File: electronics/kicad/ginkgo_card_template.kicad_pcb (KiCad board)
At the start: 4 copper layers, 100 x 100 mm, 6 parts, among them J1 GK-P, J2 GK-D

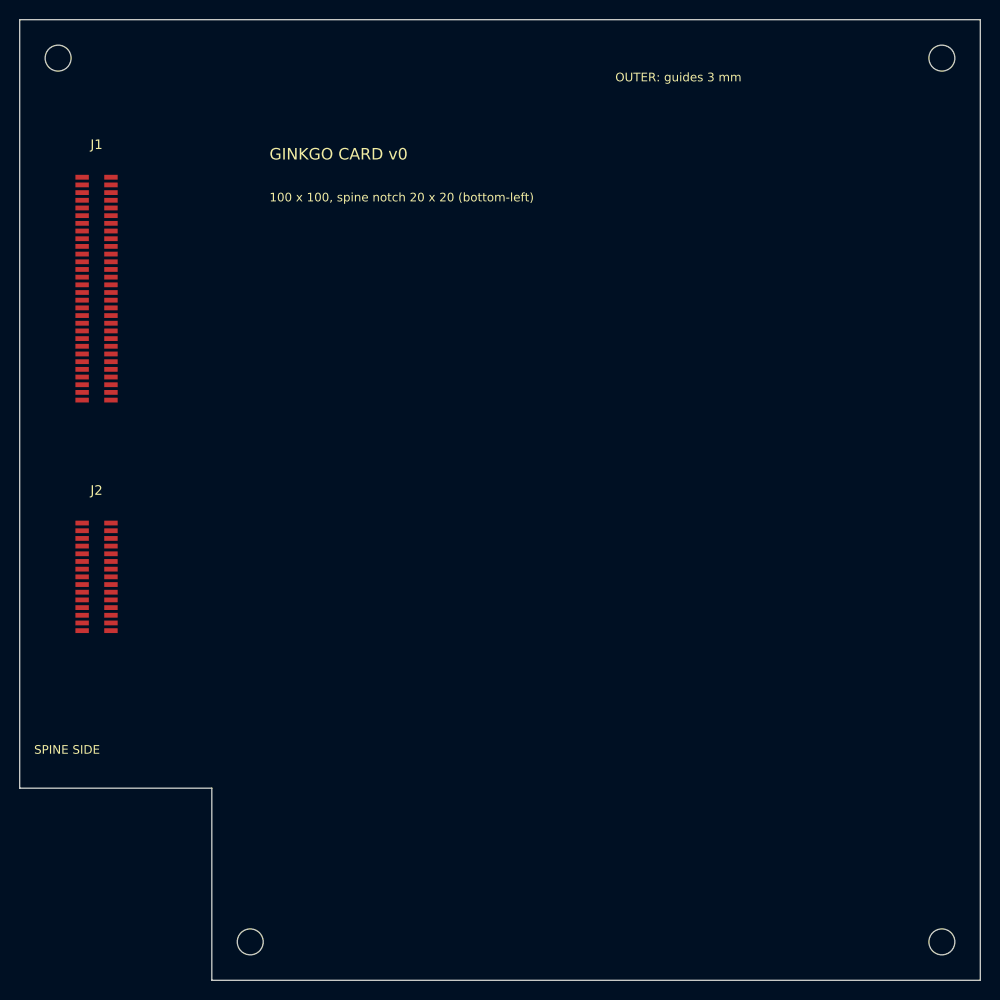
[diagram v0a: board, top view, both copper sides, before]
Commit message: Add backplane strip (KiCad, DRC clean), card format changes, EPS card specification
Pinout: distributed eFuse per card, SLOT_SEL/KILL_N hardware kill, 1.27 mm connector pitch.
Card: 4 mm backplane gap and 8 x 8 mm outer-corner relief enforced in packing and CAD.

Co-Authored-By: Claude Sonnet 5 <noreply@anthropic.com>
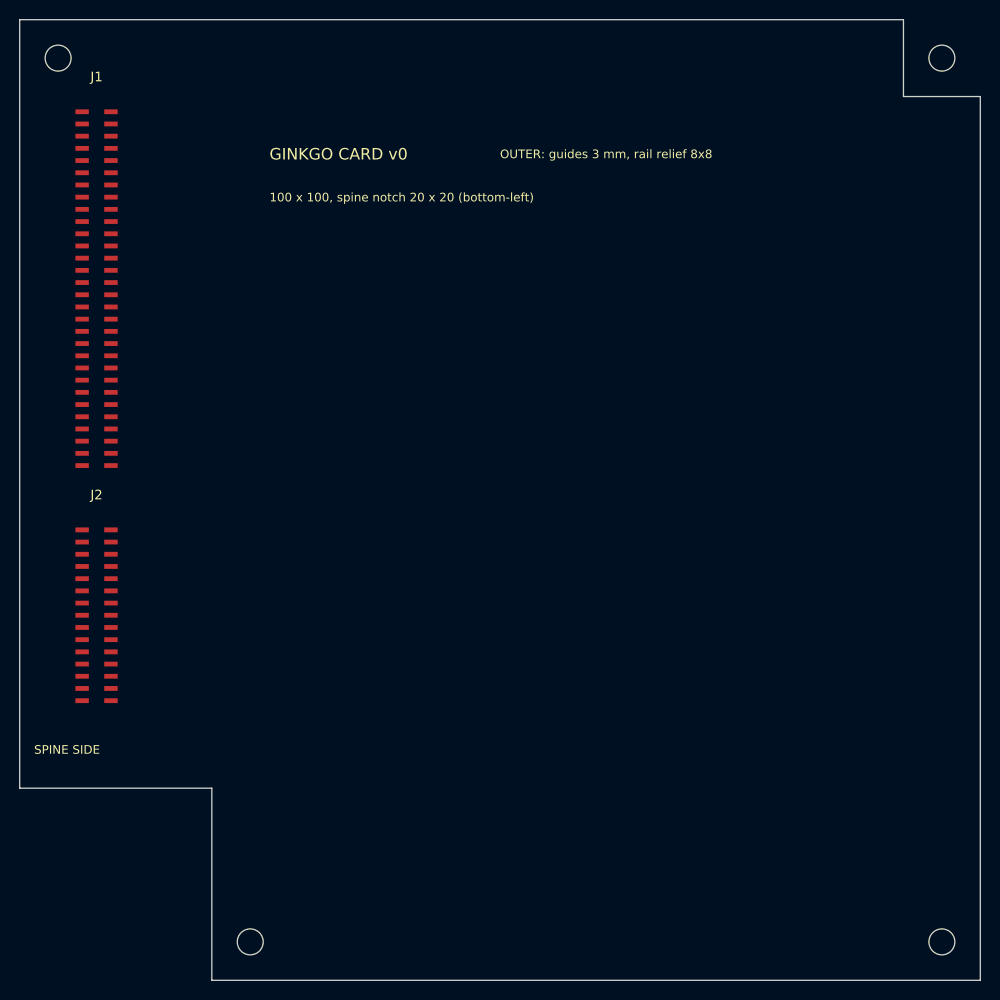
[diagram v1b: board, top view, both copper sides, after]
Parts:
- moved J2 4.00 mm to (8.00, 62.0)
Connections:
- net CARD_PRESENT_N renamed KILL_N
- net HB renamed SLOT_SEL3
- net PWR_EN renamed SLOT_SEL0
- J1 pad 34: FAULT_N -> SLOT_SEL1
- J1 pad 35: RESET_N -> SLOT_SEL2
- J1 pad 38: SPARE -> FAULT_N
- J1 pad 53: RSV -> RESET_N
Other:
- outline, holes or cut-outs redrawn
- board text added: "OUTER: guides 3 mm, rail relief 8x8"
- board text removed: "OUTER: guides 3 mm"
